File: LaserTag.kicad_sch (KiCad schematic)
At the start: 0 parts

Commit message: Added Project Outline
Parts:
- added LS1: Speaker, symbol Device:Speaker
- added SW1: SW_SPST, symbol Switch:SW_SPST
- added U1: TinyS3_Symbol, symbol TinyS3:TinyS3_Symbol
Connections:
- new net: SW1.1 (A), U1.3 (5V)
- new net: SW1.2 (B), U1.7 (IO3)
- new net: LS1.1, U1.11 (IO0)
- new net GNDREF: LS1.2, U1.14 (GND)
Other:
- note added: "Note: Ensure GPIO Pin is PWM Capable. Potentially Use Headphones Instead. (Analog Out)"
- note added: "Note: Pull-Down GPIO Pin (Digital In)"

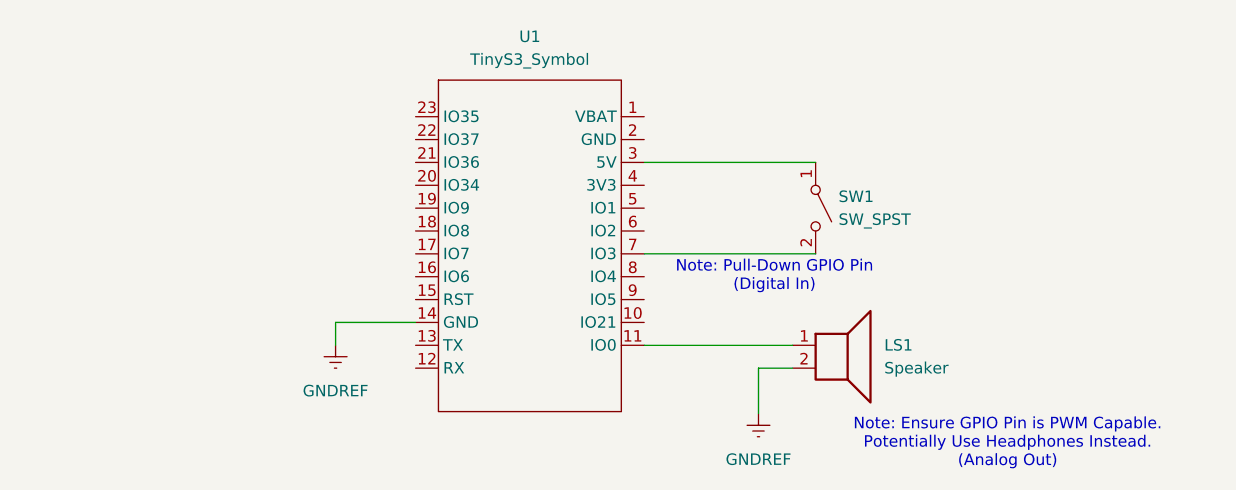
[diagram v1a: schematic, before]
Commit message: Schematic 1.0 Compelte, Passes ERC
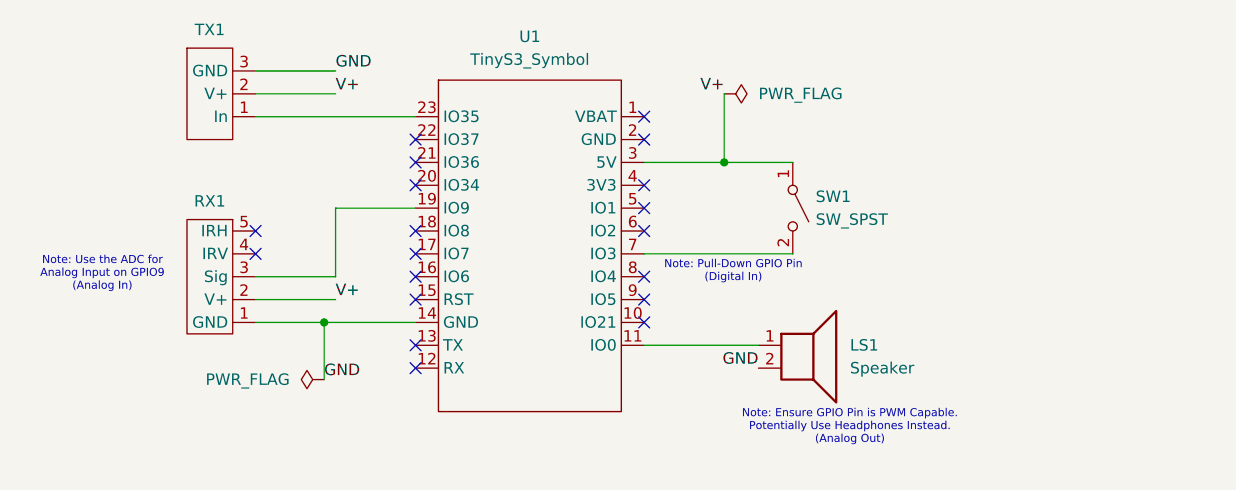
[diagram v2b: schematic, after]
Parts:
- added RX1: ~, symbol LaserTagSymbols:LaserTag_Receiver
- added TX1: ~, symbol LaserTagSymbols:LaserTag_Emitter
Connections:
- net V+: now reaches SW1.1 (A), U1.3 (5V)
- net V+: now also RX1.2 (V+), TX1.2 (V+)
- net at U1.19 (IO9): now also RX1.3 (Sig)
- net at U1.23 (IO35): now also TX1.1 (In)
- net GNDREF renamed GND
- net GND: now also RX1.1 (GND), TX1.3 (GND)
- no-connect marks 0 -> 19
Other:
- note added: "Note: Use the ADC for Analog Input on GPIO9 (Analog In)"
- moved on the sheet: LS1, SW1

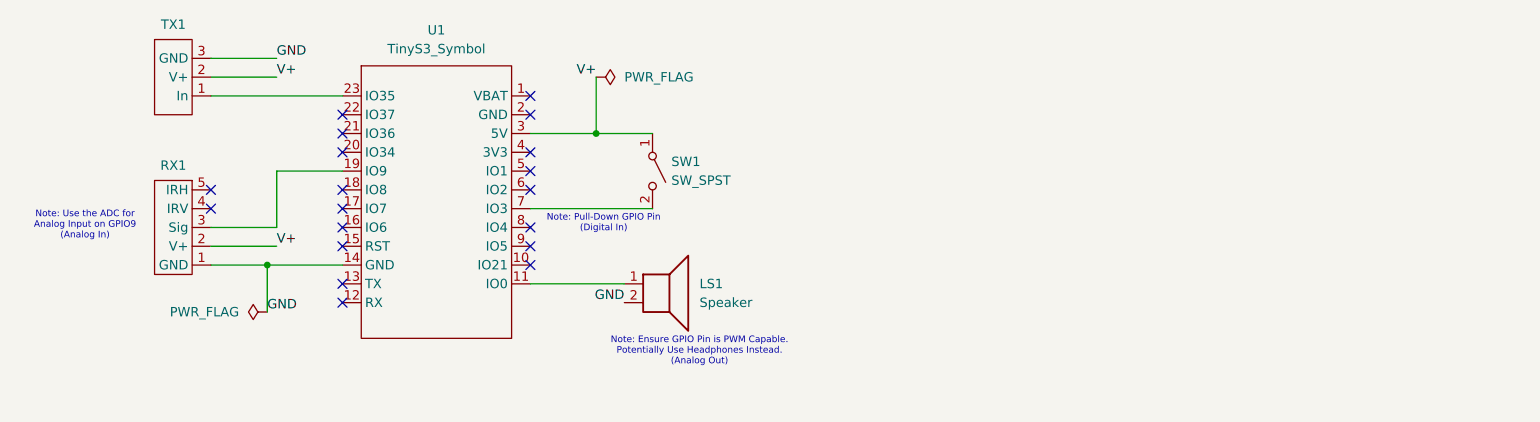
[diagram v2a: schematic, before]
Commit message: Added Comparator Logic to Receiver Schematic
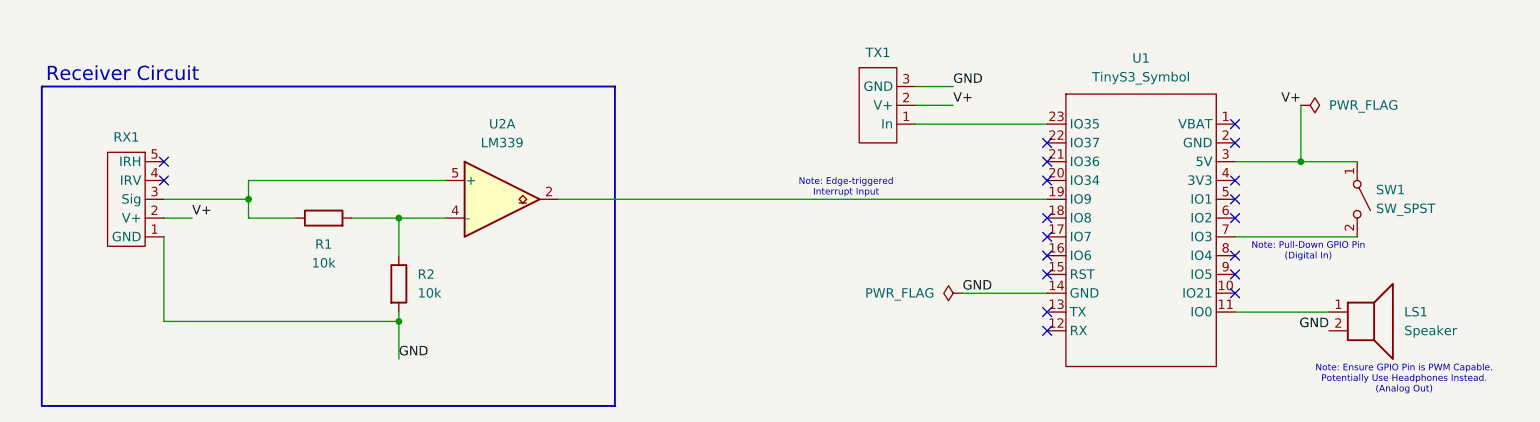
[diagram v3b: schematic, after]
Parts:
- added R1, R2: 10k, symbol Device:R
- added U2: LM339, symbol Comparator:LM339
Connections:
- net GND: now also R2.2
- net at RX1.3 (Sig): now also R1.1, U2.5 (+); no longer U1.19 (IO9)
- new net: R1.2, R2.1, U2.4 (-)
- new net: U1.19 (IO9), U2.2
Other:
- note added: "Note: Edge-triggered Interrupt Input"
- note added: "Receiver Circuit"
- note removed: "Note: Use the ADC for Analog Input on GPIO9 (Analog In)"
- moved on the sheet: LS1, RX1, SW1, TX1, U1

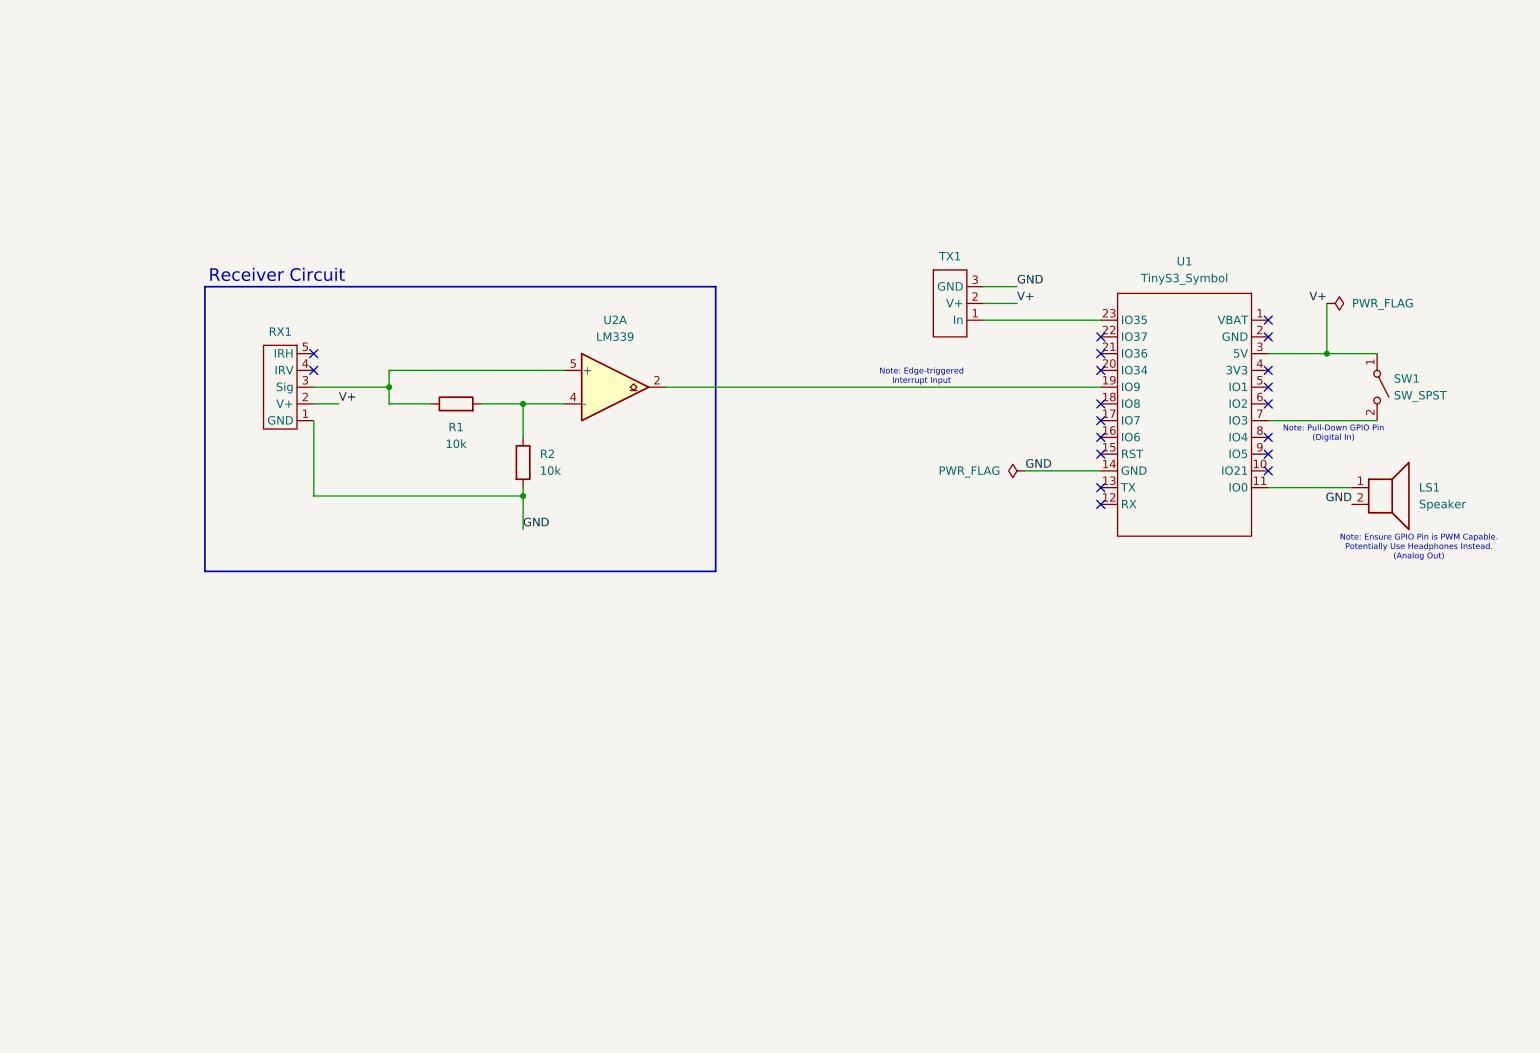
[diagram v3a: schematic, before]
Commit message: Added Aux Header Symbol + Organization
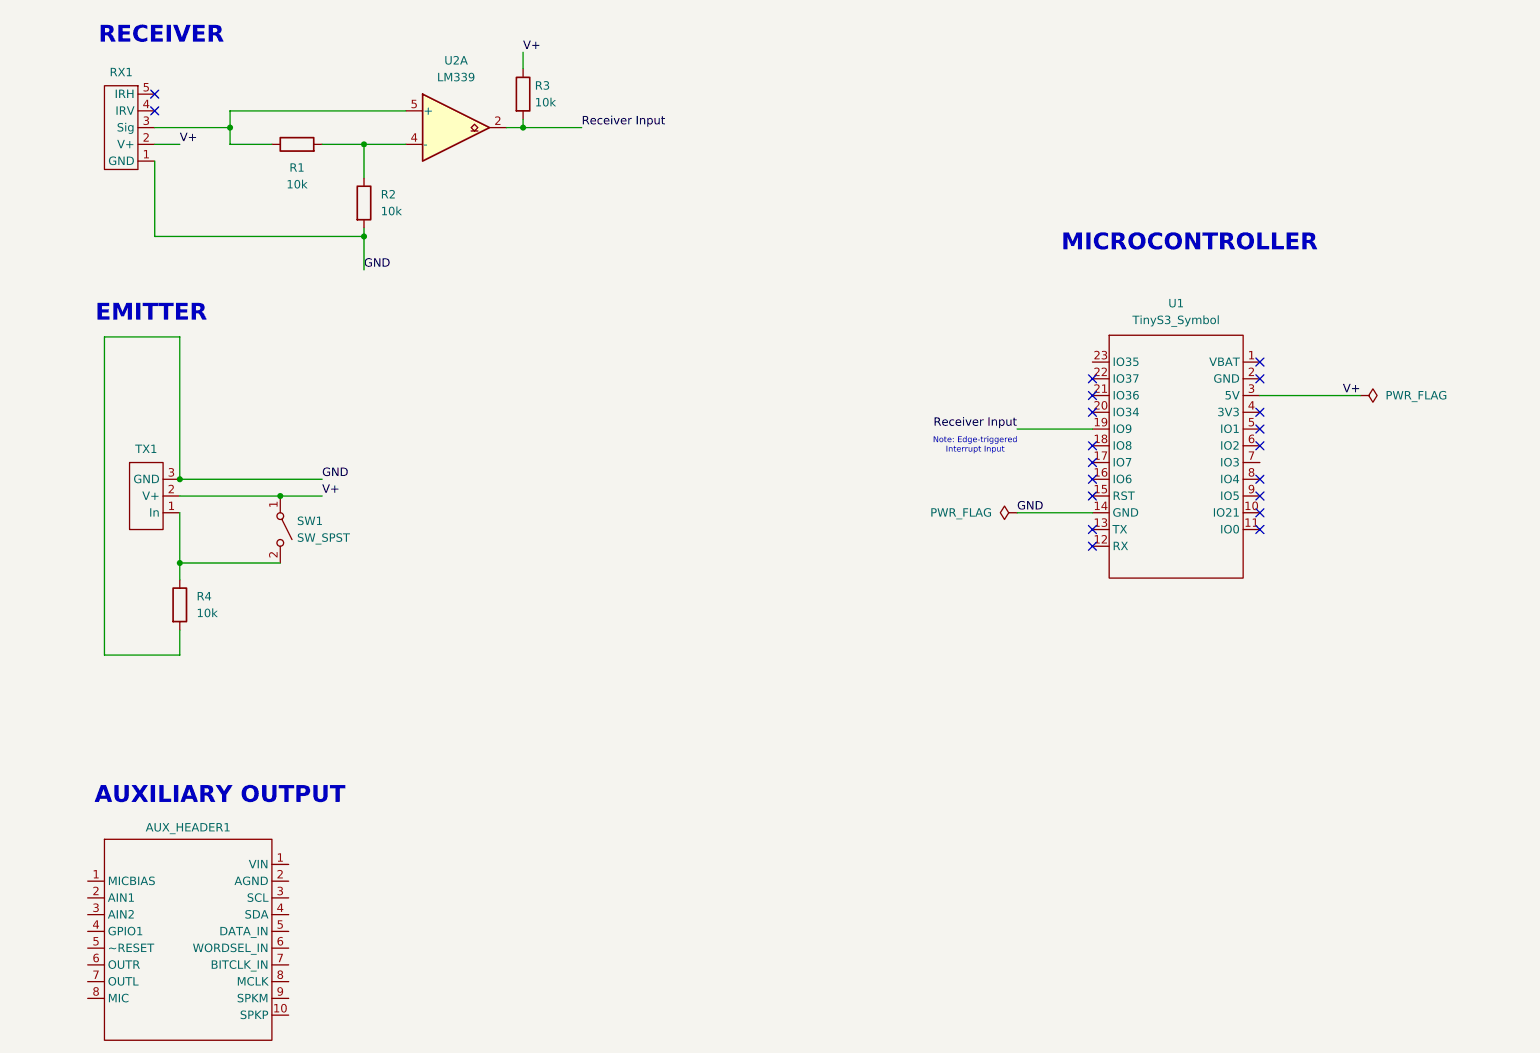
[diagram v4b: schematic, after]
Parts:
- removed LS1: Speaker, symbol Device:Speaker
- added AUX_HEADER1: ~, symbol LaserTagSymbols:LaserTag_Aux_Header
- added R3, R4: 10k, symbol Device:R
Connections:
- net GND: now also R4.2
- net V+: now also R3.1
- net at SW1.2 (B): now also TX1.1 (In), R4.1; no longer U1.7 (IO3)
- net at U1.23 (IO35): no longer TX1.1 (In)
- net Receiver Input: now reaches U1.19 (IO9), U2.2
- net Receiver Input: now also R3.2
- no-connect marks 19 -> 20
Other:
- note added: "AUXILIARY OUTPUT"
- note added: "EMITTER"
- note added: "MICROCONTROLLER"
- note added: "RECEIVER"
- note removed: "Note: Ensure GPIO Pin is PWM Capable. Potentially Use Headphones Instead. (Analog Out)"
- note removed: "Note: Pull-Down GPIO Pin (Digital In)"
- note removed: "Receiver Circuit"
- moved on the sheet: R1, R2, RX1, SW1, TX1, U1, U2A

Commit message: Updated emitter Schematic.
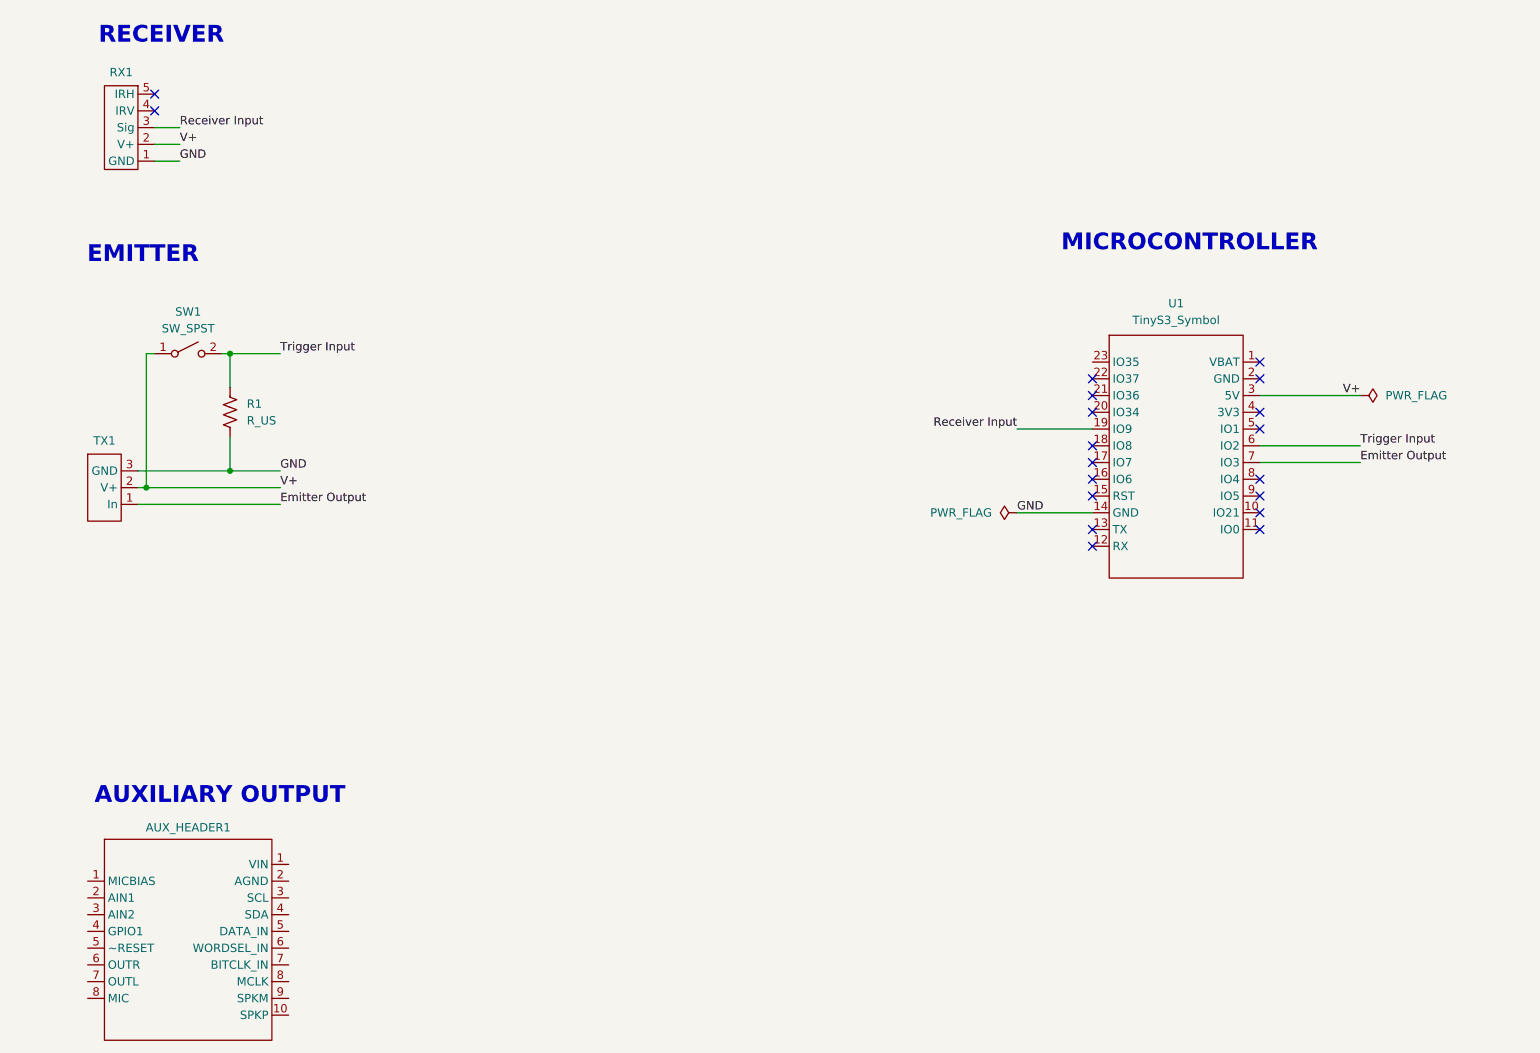
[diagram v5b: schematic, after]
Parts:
- removed R1, R2, R3, R4: 10k, symbol Device:R
- removed U2: LM339, symbol Comparator:LM339
- added R1: R_US, symbol Device:R_US
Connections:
- net GND: now also R1.2
- net Receiver Input: now also RX1.3 (Sig)
- net Emitter Output: now reaches TX1.1 (In)
- net Emitter Output: now also U1.7 (IO3); no longer SW1.2 (B)
- net Trigger Input: now reaches U1.6 (IO2)
- net Trigger Input: now also SW1.2 (B), R1.1
- no-connect marks 20 -> 19
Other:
- note removed: "Note: Edge-triggered Interrupt Input"
- moved on the sheet: SW1, TX1

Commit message: Added I2S DAC Headphone Out to Schematic
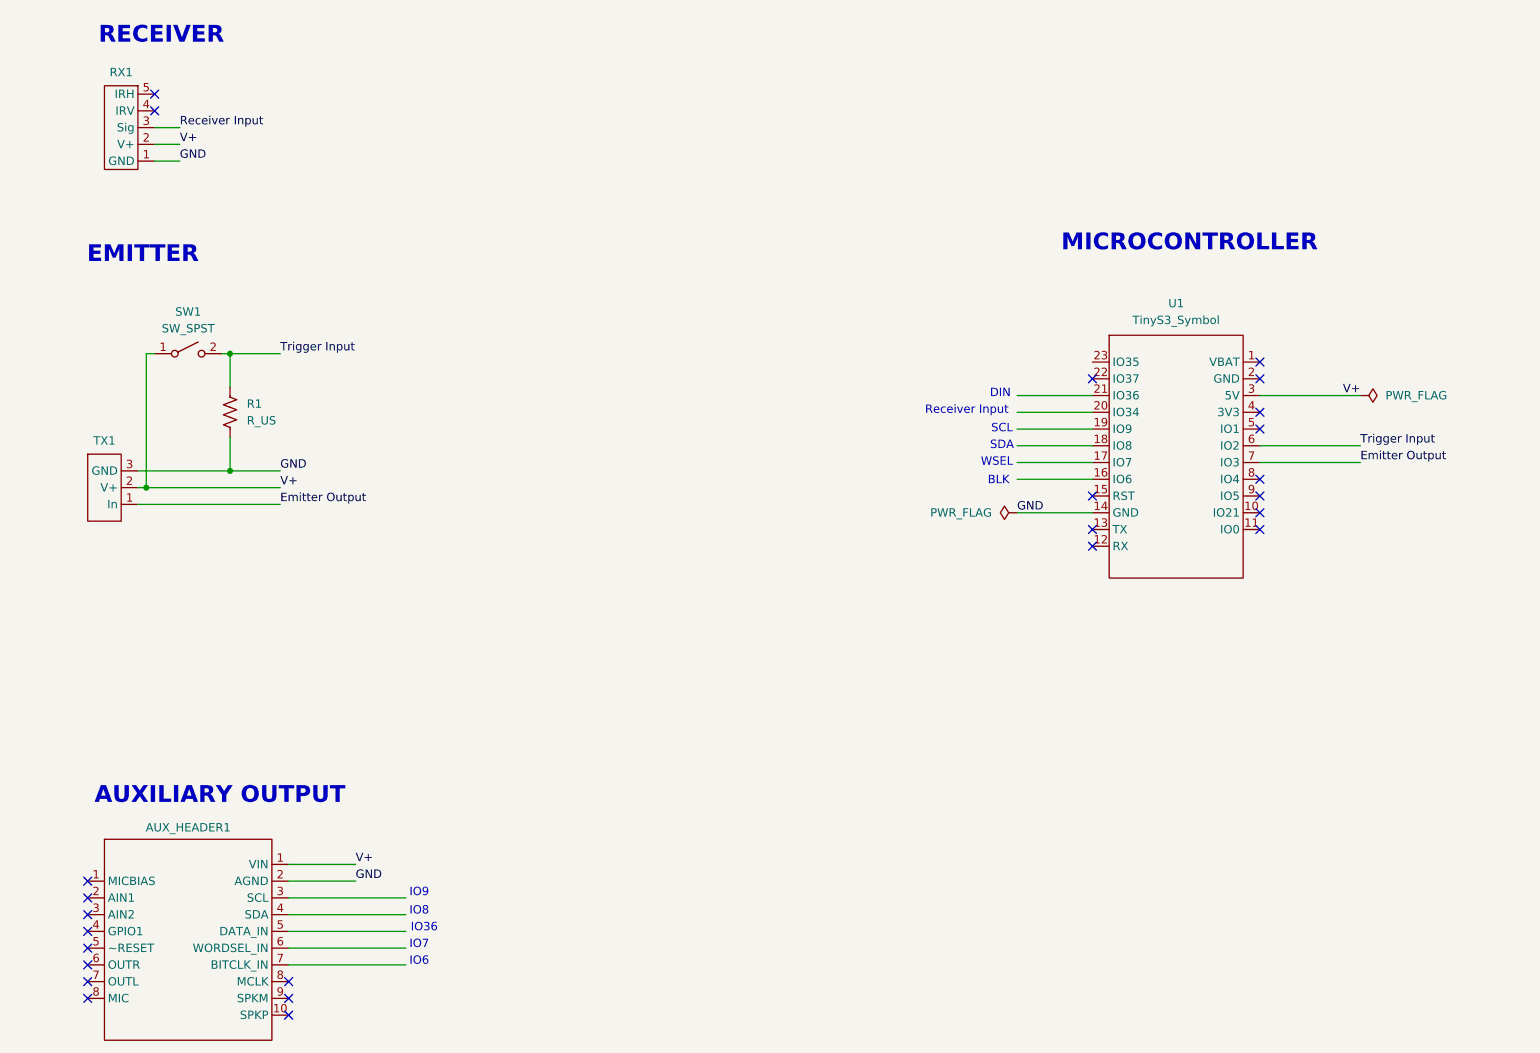
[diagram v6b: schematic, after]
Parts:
- AUX_HEADER1, RX1, TX1: value ~ -> (none)
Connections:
- net GND: now also AUX_HEADER1.2 (AGND)
- net Receiver Input: no longer U1.19 (IO9)
- net V+: now also AUX_HEADER1.1 (VIN)
- no-connect marks 19 -> 25
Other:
- note added: "BLK"
- note added: "DIN"
- note added: "IO36"
- note added: "IO6"
- note added: "IO7"
- note added: "IO8"
- note added: "IO9"
- note added: "Receiver Input"
- note added: "SCL"
- note added: "SDA"
- note added: "WSEL"
